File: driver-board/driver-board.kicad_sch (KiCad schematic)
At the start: 54 parts, among them J1 MCP4725, J2 Conn_Coaxial, J3 MCP4725, J4 Conn_Coaxial, SW1 RST, SW2 BIAS ON/OF, U1 Pico, U2 MIC5317, U3 TSV358, U4 TSV358, U5 TCBT-2R5G, U6 LM2904, U7 LT3462A

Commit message: fixed RN1 fp
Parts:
- RN1: footprint Resistor_SMD:R_Array_Convex_4x1206 -> lib:ACASA5002S5002P1AT
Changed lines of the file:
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@@
       (effects (font (size 1.27 1.27)) hide)
     )
-    (property "Footprint" "Resistor_SMD:R_Array_Convex_4x1206" (id 2) (at 66.04 90.678 90)
+    (property "Footprint" "lib:ACASA5002S5002P1AT" (id 2) (at 66.04 90.678 90)
       (effects (font (size 1.27 1.27)) hide)
     )
@@
       (effects (font (size 1.27 1.27)) hide)
     )
-    (property "Footprint" "Resistor_SMD:R_Array_Convex_4x1206" (id 2) (at 73.66 112.522 90)
+    (property "Footprint" "lib:ACASA5002S5002P1AT" (id 2) (at 73.66 112.522 90)
       (effects (font (size 1.27 1.27)) hide)
     )
@@
       (effects (font (size 1.27 1.27)) hide)
     )
-    (property "Footprint" "Resistor_SMD:R_Array_Convex_4x1206" (id 2) (at 82.55 80.772 90)
+    (property "Footprint" "lib:ACASA5002S5002P1AT" (id 2) (at 82.55 80.772 90)
       (effects (font (size 1.27 1.27)) hide)
     )
@@
       (effects (font (size 1.27 1.27)) hide)
     )
-    (property "Footprint" "Resistor_SMD:R_Array_Convex_4x1206" (id 2) (at 63.5 95.758 90)
+    (property "Footprint" "lib:ACASA5002S5002P1AT" (id 2) (at 63.5 95.758 90)
       (effects (font (size 1.27 1.27)) hide)
     )
@@
     )
     (path "/ccf42105-7c88-40e9-acfe-aba673874876"
-      (reference "RN1") (unit 1) (value "R_Pack04_SIP_Split") (footprint "Resistor_SMD:R_Array_Convex_4x1206")
+      (reference "RN1") (unit 1) (value "R_Pack04_SIP_Split") (footprint "lib:ACASA5002S5002P1AT")
     )
     (path "/456ac708-52ba-4de4-b300-dc30b320a854"
-      (reference "RN1") (unit 2) (value "R_Pack04_SIP_Split") (footprint "Resistor_SMD:R_Array_Convex_4x1206")
+      (reference "RN1") (unit 2) (value "R_Pack04_SIP_Split") (footprint "lib:ACASA5002S5002P1AT")
     )
     (path "/aee5fe8e-e7c3-472d-872f-1329481d79a9"
-      (reference "RN1") (unit 3) (value "R_Pack04_SIP_Split") (footprint "Resistor_SMD:R_Array_Convex_4x1206")
+      (reference "RN1") (unit 3) (value "R_Pack04_SIP_Split") (footprint "lib:ACASA5002S5002P1AT")
     )
     (path "/f394be56-be3c-42a7-a975-55b240b92972"
-      (reference "RN1") (unit 4) (value "R_Pack04_SIP_Split") (footprint "Resistor_SMD:R_Array_Convex_4x1206")
+      (reference "RN1") (unit 4) (value "R_Pack04_SIP_Split") (footprint "lib:ACASA5002S5002P1AT")
     )
     (path "/2f4e6d3b-e788-40fd-a30d-623725dbb33b"

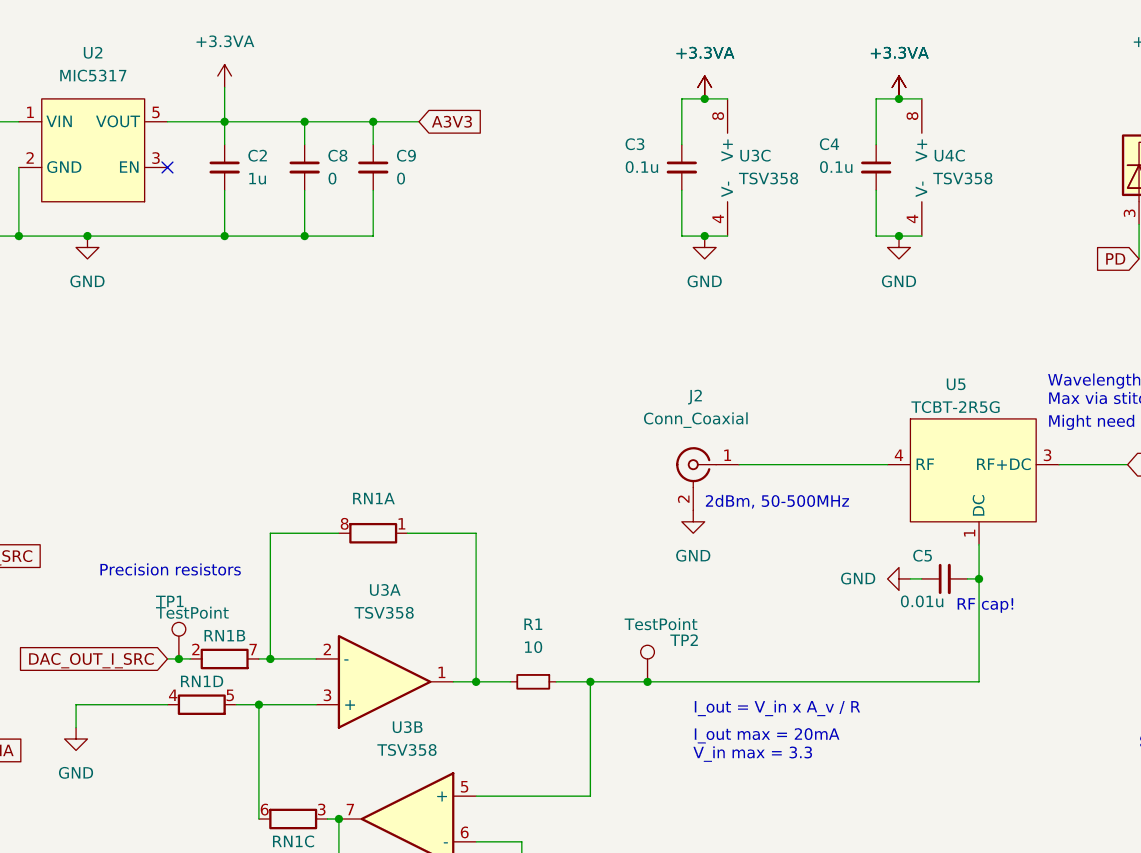
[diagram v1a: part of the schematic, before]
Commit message: fixed U2-EN pin
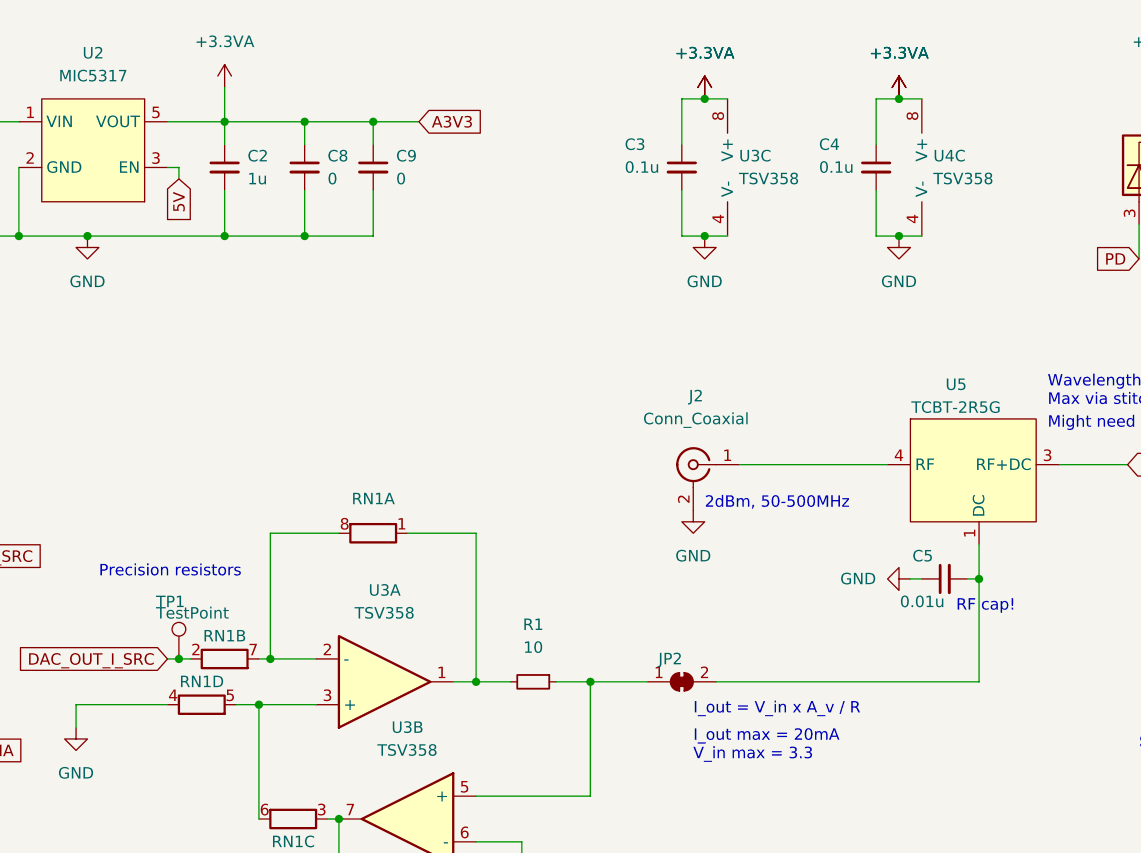
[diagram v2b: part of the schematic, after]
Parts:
- removed TP2: TestPoint, TestPoint:TestPoint_Pad_D1.5mm, symbol Connector:TestPoint
- added JP2: SolderJumper_2_Bridged, Jumper:SolderJumper-2_P1.3mm_Bridged_Pad1.0x1.5mm, symbol Jumper:SolderJumper_2_Bridged
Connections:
- net 5V: now also U2.3 (EN)
- net at C5.2, U5.1 (DC): now also JP2.2 (B); no longer R1.1, U3.5 (+)
- new net: JP2.1 (A), R1.1, U3.5 (+)
- no-connect marks 4 -> 3
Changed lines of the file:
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@@
   (junction (at 130.81 123.19) (diameter 0) (color 0 0 0 0)
-  )
-  (junction (at 113.03 95.25) (diameter 0) (color 0 0 0 0)
   )
   (junction (at 267.97 73.66) (diameter 0) (color 0 0 0 0)
@@
   (no_connect (at 209.55 53.34))
   (no_connect (at 224.79 50.8))
-  (no_connect (at 59.69 38.1))
   (wire (pts (xy 66.04 33.02) (xy 74.93 33.02))
     (stroke (width 0) (type default) (color 0 0 0 0))
@@
     (stroke (width 0) (type default) (color 0 0 0 0))
   )
+  (wire (pts (xy 60.96 38.1) (xy 60.96 39.37))
+    (stroke (width 0) (type default) (color 0 0 0 0))
+  )
   (wire (pts (xy 74.93 40.64) (xy 74.93 45.72))
     (stroke (width 0) (type default) (color 0 0 0 0))
@@
     (stroke (width 0) (type default) (color 0 0 0 0))
   )
+  (wire (pts (xy 59.69 38.1) (xy 60.96 38.1))
+    (stroke (width 0) (type default) (color 0 0 0 0))
+  )
   (wire (pts (xy 116.84 30.48) (xy 119.38 30.48))
     (stroke (width 0) (type default) (color 0 0 0 0))
@@
     (stroke (width 0) (type default) (color 0 0 0 0))
   )
+  (wire (pts (xy 120.65 95.25) (xy 149.86 95.25))
+    (stroke (width 0) (type default) (color 0 0 0 0))
+  )
   (wire (pts (xy 261.62 73.66) (xy 257.81 73.66))
     (stroke (width 0) (type default) (color 0 0 0 0))
@@
     (stroke (width 0) (type default) (color 0 0 0 0))
   )
-  (wire (pts (xy 113.03 95.25) (xy 149.86 95.25))
+  (wire (pts (xy 106.68 95.25) (xy 113.03 95.25))
     (stroke (width 0) (type default) (color 0 0 0 0))
   )
@@
   )
   (wire (pts (xy 194.31 114.3) (xy 204.47 114.3))
-    (stroke (width 0) (type default) (color 0 0 0 0))
-  )
-  (wire (pts (xy 106.68 95.25) (xy 113.03 95.25))
     (stroke (width 0) (type default) (color 0 0 0 0))
   )
@@
     (property "Intersheet References" "${INTERSHEET_REFS}" (id 0) (at 280.1802 73.5806 0)
       (effects (font (size 1.27 1.27)) (justify left) hide)
+    )
+  )
+  (global_label "5V" (shape input) (at 60.96 39.37 270) (fields_autoplaced)
+    (effects (font (size 1.27 1.27)) (justify right))
+    (property "Intersheet References" "${INTERSHEET_REFS}" (id 0) (at 60.8806 44.0812 90)
+      (effects (font (size 1.27 1.27)) (justify right) hide)
     )
   )
@@
     (pin "2")
   )
+  (symbol (lib_id "Jumper:SolderJumper_2_Bridged") (at 116.84 95.25 0) (unit 1)
+    (in_bom yes) (on_board yes)
+    (property "Reference" "JP2" (id 0) (at 115.57 92.71 0))
+    (property "Value" "SolderJumper_2_Bridged" (id 1) (at 116.84 91.44 0)
+      (effects (font (size 1.27 1.27)) hide)
+    )
+    (property "Footprint" "Jumper:SolderJumper-2_P1.3mm_Bridged_Pad1.0x1.5mm" (id 2) (at 116.84 95.25 0)
+      (effects (font (size 1.27 1.27)) hide)
+    )
+    (property "Datasheet" "~" (id 3) (at 116.84 95.25 0)
+      (effects (font (size 1.27 1.27)) hide)
+    )
+    (pin "1")
+    (pin "2")
+  )
   (symbol (lib_id "Connector:TestPoint") (at 237.49 156.21 270) (unit 1)
     (in_bom yes) (on_board yes)
@@
     (pin "1")
   )
-  (symbol (lib_id "Connector:TestPoint") (at 113.03 95.25 0) (unit 1)
-    (in_bom yes) (on_board yes)
-    (property "Reference" "TP2" (id 0) (at 115.57 90.6779 0)
-      (effects (font (size 1.27 1.27)) (justify left))
-    )
-    (property "Value" "TestPoint" (id 1) (at 110.49 88.9 0)
-      (effects (font (size 1.27 1.27)) (justify left))
-    )
-    (property "Footprint" "TestPoint:TestPoint_Pad_D1.5mm" (id 2) (at 118.11 95.25 0)
-      (effects (font (size 1.27 1.27)) hide)
-    )
-    (property "Datasheet" "~" (id 3) (at 118.11 95.25 0)
-      (effects (font (size 1.27 1.27)) hide)
-    )
-    (pin "1")
-  )
   (symbol (lib_id "Device:C_Small") (at 82.55 38.1 0) (unit 1)
     (in_bom yes) (on_board yes) (fields_autoplaced)
@@
       (reference "JP1") (unit 1) (value "SolderJumper_2_Open") (footprint "Jumper:SolderJumper-2_P1.3mm_Bridged_Pad1.0x1.5mm")
     )
+    (path "/4fd04d76-bcdf-4e8c-9ee9-52f4b923099d"
+      (reference "JP2") (unit 1) (value "SolderJumper_2_Bridged") (footprint "Jumper:SolderJumper-2_P1.3mm_Bridged_Pad1.0x1.5mm")
+    )
     (path "/10ca3d81-dd36-472a-82b4-537fac0875d5"
       (reference "L1") (unit 1) (value "22u") (footprint "Inductor_SMD:L_1210_3225Metric_Pad1.42x2.65mm_HandSolder")
@@
       (reference "TP1") (unit 1) (value "TestPoint") (footprint "TestPoint:TestPoint_Pad_D1.5mm")
     )
-    (path "/b4c22fe8-8aa5-47c4-8799-9218583011ac"
-      (reference "TP2") (unit 1) (value "TestPoint") (footprint "TestPoint:TestPoint_Pad_D1.5mm")
-    )
     (path "/cee34a43-b4c9-4a9e-84b4-1fc8fae03e8e"

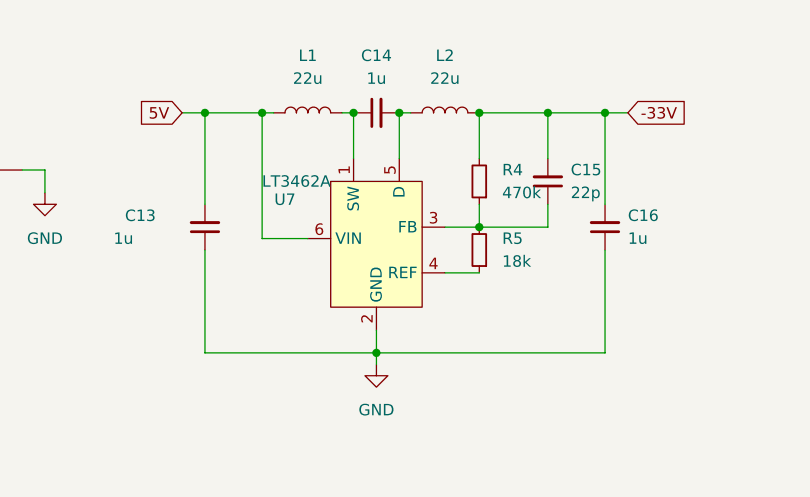
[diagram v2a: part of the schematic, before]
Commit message: fixed lt3462 fp, routing pending
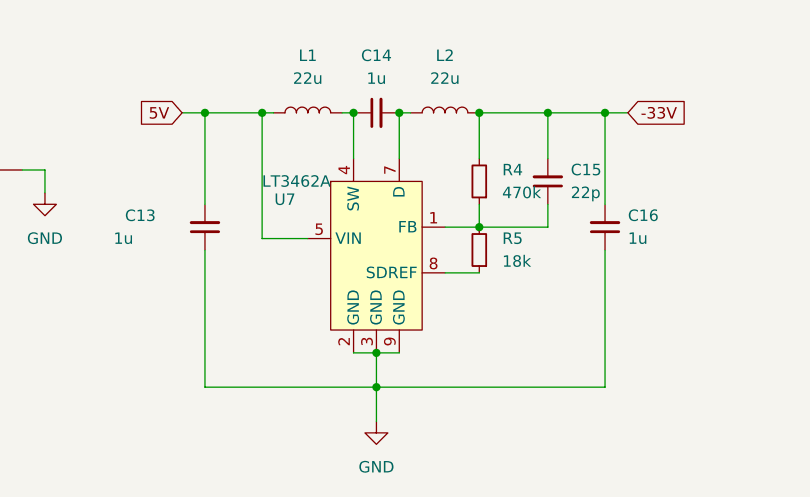
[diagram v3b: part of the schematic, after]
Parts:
- U7: footprint Package_TO_SOT_SMD:TSOT-23-6 -> lib:LT3462A
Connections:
- net 5V: now also U7.5 (VIN); no longer U7.6 (VIN)
- net GND: now also U7.3 (GND), U7.9 (GND)
- net at C15.1, R4.1, R5.2: now also U7.1 (FB); no longer U7.3 (FB)
- net at C14.1, L1.2: now also U7.4 (SW); no longer U7.1 (SW)
- net at R5.1: now also U7.8 (SDREF); no longer U7.4 (REF)
- net at C14.2, L2.1: now also U7.7 (D); no longer U7.5 (D)
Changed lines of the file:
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@@
   (junction (at 151.13 166.37) (diameter 0) (color 0 0 0 0)
+  )
+  (junction (at 139.7 184.15) (diameter 0) (color 0 0 0 0)
   )
   (junction (at 217.17 119.38) (diameter 0) (color 0 0 0 0)
@@
     (stroke (width 0) (type default) (color 0 0 0 0))
   )
-  (wire (pts (xy 120.65 168.91) (xy 120.65 180.34))
+  (wire (pts (xy 120.65 168.91) (xy 120.65 184.15))
     (stroke (width 0) (type default) (color 0 0 0 0))
   )
@@
     (stroke (width 0) (type default) (color 0 0 0 0))
   )
+  (wire (pts (xy 165.1 184.15) (xy 139.7 184.15))
+    (stroke (width 0) (type default) (color 0 0 0 0))
+  )
   (wire (pts (xy 143.51 45.72) (xy 140.97 45.72))
     (stroke (width 0) (type default) (color 0 0 0 0))
   )
+  (wire (pts (xy 120.65 184.15) (xy 139.7 184.15))
+    (stroke (width 0) (type default) (color 0 0 0 0))
+  )
   (wire (pts (xy 233.68 76.2) (xy 238.76 76.2))
     (stroke (width 0) (type default) (color 0 0 0 0))
@@
     (stroke (width 0) (type default) (color 0 0 0 0))
   )
+  (wire (pts (xy 137.16 180.34) (xy 139.7 180.34))
+    (stroke (width 0) (type default) (color 0 0 0 0))
+  )
   (wire (pts (xy 266.7 114.3) (xy 270.51 114.3))
     (stroke (width 0) (type default) (color 0 0 0 0))
   )
-  (wire (pts (xy 120.65 180.34) (xy 139.7 180.34))
-    (stroke (width 0) (type default) (color 0 0 0 0))
-  )
   (wire (pts (xy 261.62 121.92) (xy 261.62 124.46))
     (stroke (width 0) (type default) (color 0 0 0 0))
@@
     (stroke (width 0) (type default) (color 0 0 0 0))
   )
-  (wire (pts (xy 139.7 180.34) (xy 139.7 181.61))
+  (wire (pts (xy 139.7 180.34) (xy 139.7 184.15))
     (stroke (width 0) (type default) (color 0 0 0 0))
   )
@@
     (stroke (width 0) (type default) (color 0 0 0 0))
   )
-  (wire (pts (xy 165.1 180.34) (xy 165.1 168.91))
+  (wire (pts (xy 165.1 168.91) (xy 165.1 184.15))
     (stroke (width 0) (type default) (color 0 0 0 0))
   )
@@
     (stroke (width 0) (type default) (color 0 0 0 0))
   )
-  (wire (pts (xy 139.7 177.8) (xy 139.7 180.34))
-    (stroke (width 0) (type default) (color 0 0 0 0))
-  )
   (wire (pts (xy 93.98 107.95) (xy 106.68 107.95))
     (stroke (width 0) (type default) (color 0 0 0 0))
@@
     (stroke (width 0) (type default) (color 0 0 0 0))
   )
+  (wire (pts (xy 139.7 184.15) (xy 139.7 187.96))
+    (stroke (width 0) (type default) (color 0 0 0 0))
+  )
   (wire (pts (xy 143.51 30.48) (xy 140.97 30.48))
     (stroke (width 0) (type default) (color 0 0 0 0))
   )
-  (wire (pts (xy 139.7 180.34) (xy 165.1 180.34))
+  (wire (pts (xy 139.7 180.34) (xy 142.24 180.34))
     (stroke (width 0) (type default) (color 0 0 0 0))
   )
@@
     (property "Reference" "U7" (id 0) (at 129.54 163.3093 0))
     (property "Value" "LT3462A" (id 1) (at 130.81 161.29 0))
-    (property "Footprint" "Package_TO_SOT_SMD:TSOT-23-6" (id 2) (at 142.24 153.67 0)
+    (property "Footprint" "lib:LT3462A" (id 2) (at 142.24 153.67 0)
       (effects (font (size 1.27 1.27)) hide)
     )
@@
     (pin "5")
     (pin "6")
-  )
-  (symbol (lib_id "power:GND") (at 139.7 181.61 0) (unit 1)
-    (in_bom yes) (on_board yes) (fields_autoplaced)
-    (property "Reference" "#PWR0101" (id 0) (at 139.7 187.96 0)
-      (effects (font (size 1.27 1.27)) hide)
-    )
-    (property "Value" "GND" (id 1) (at 139.7 186.69 0))
-    (property "Footprint" "" (id 2) (at 139.7 181.61 0)
-      (effects (font (size 1.27 1.27)) hide)
-    )
-    (property "Datasheet" "" (id 3) (at 139.7 181.61 0)
+    (pin "7")
+    (pin "8")
+    (pin "9")
+  )
+  (symbol (lib_id "power:GND") (at 139.7 187.96 0) (unit 1)
+    (in_bom yes) (on_board yes) (fields_autoplaced)
+    (property "Reference" "#PWR0101" (id 0) (at 139.7 194.31 0)
+      (effects (font (size 1.27 1.27)) hide)
+    )
+    (property "Value" "GND" (id 1) (at 139.7 193.04 0))
+    (property "Footprint" "" (id 2) (at 139.7 187.96 0)
+      (effects (font (size 1.27 1.27)) hide)
+    )
+    (property "Datasheet" "" (id 3) (at 139.7 187.96 0)
       (effects (font (size 1.27 1.27)) hide)
     )
@@
     )
     (path "/8bb3365e-a398-4afc-9d2a-e3437d8b58de"
-      (reference "U7") (unit 1) (value "LT3462A") (footprint "Package_TO_SOT_SMD:TSOT-23-6")
-    )
-  )
+      (reference "U7") (unit 1) (value "LT3462A") (footprint "lib:LT3462A")
+    )
+  )
